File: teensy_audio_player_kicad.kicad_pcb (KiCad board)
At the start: 2 copper layers, 53.3 x 45.7 mm, 14 parts, among them J1 Conn_02x13_Odd_Even, J2 Conn_01x03_Female, J3 Conn_01x09_Male, Q1 2N3904, U1 Teensy3.6, U2 74LS373, U3 I2S_DAC

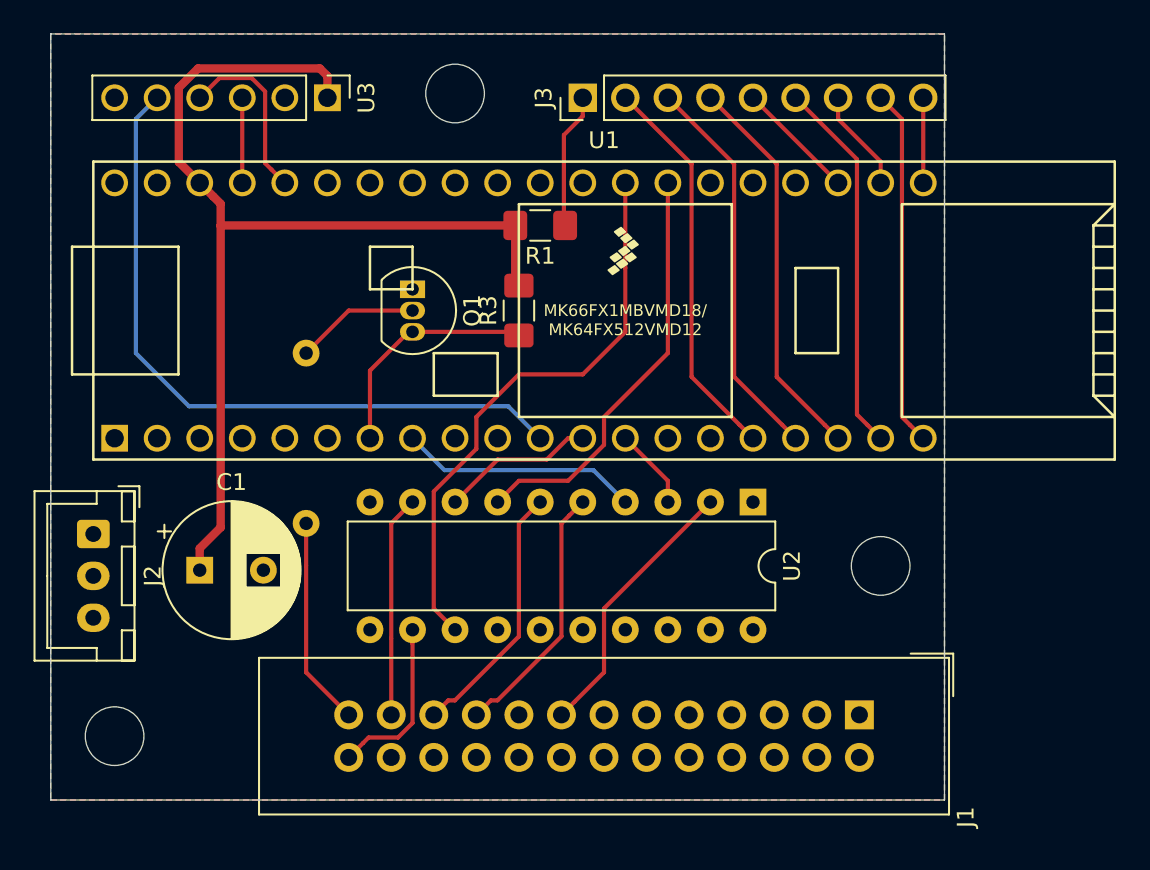
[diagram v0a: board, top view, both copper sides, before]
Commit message: update PCB for new version with teensy41
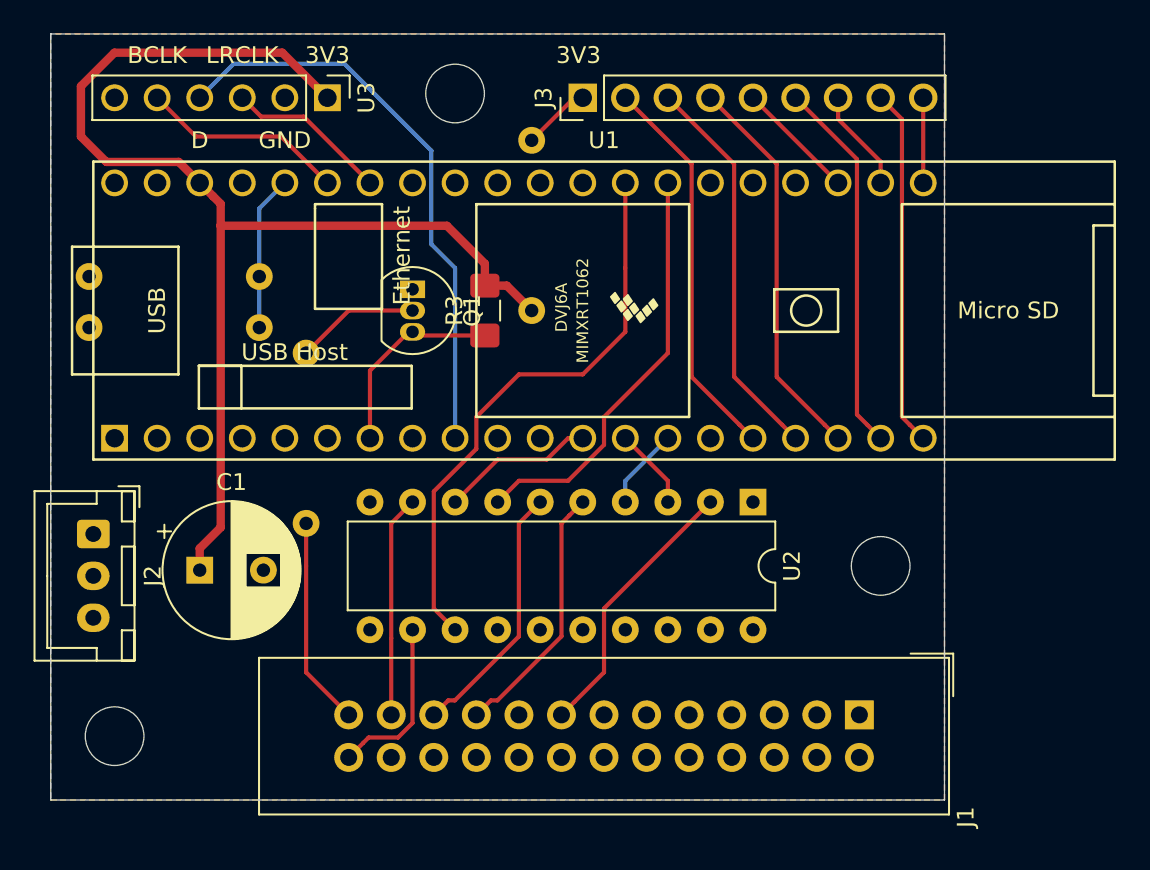
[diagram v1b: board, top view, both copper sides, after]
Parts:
- added R4: R-Device, Resistor_THT:R_Axial_DIN0207_L6.3mm_D2.5mm_P10.16mm_Horizontal, B.Cu at (88.6, 70.4)
- added R5: R-Device, Resistor_THT:R_Axial_DIN0207_L6.3mm_D2.5mm_P10.16mm_Horizontal, B.Cu at (88.6, 73.4)
- R1: footprint Resistor_SMD:R_1206_3216Metric_Pad1.42x1.75mm_HandSolder -> Resistor_THT:R_Axial_DIN0207_L6.3mm_D2.5mm_P10.16mm_Horizontal; moved to B.Cu
- U1: value Teensy3.6 -> Teensy4.1; footprint teensy_audio_player_kicad:Teensy35_36 -> teensy_audio_player_kicad:Teensy41
- moved R1 5.11 mm to (104.9, 72.4), turned to 90 degrees
- moved R3 2.03 mm to (102.1, 72.4)
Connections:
- net Net-(J3-Pad2) renamed /24
- net Net-(J3-Pad3) renamed /25
- net Net-(J3-Pad4) renamed /26
- net Net-(J3-Pad6) renamed /27
- net Net-(J3-Pad8) renamed /28
- net Net-(U1-Pad12) renamed /CS
- net Net-(U1-Pad13) renamed /MOSI
- J3 pad 5: Net-(J3-Pad5) -> /39
- J3 pad 7: Net-(J3-Pad7) -> /38
- J3 pad 9: Net-(J3-Pad9) -> /37
- R1 pad 1: Net-(J3-Pad1) -> +3V3
- R1 pad 2: +3V3 -> Net-(J3-Pad1)
- U1 pad 14: Net-(U1-Pad14) -> /CMD_DATA
- U1 pad 34: Net-(J3-Pad9) -> GND
- U1 pad 35: Net-(J3-Pad7) -> /SCK
- U1 pad 36: Net-(J3-Pad5) -> /RST
- U1 pad 39: GND -> Net-(U1-Pad39)
- U1 pad 46: Net-(U1-Pad46) -> +3V3
- U1 pad 47: Net-(U1-Pad47) -> GND
- U1 pad 48: Net-(U1-Pad48) -> VCC
- U2 pad 13: Net-(U1-Pad41) -> /RST
- U2 pad 4: Net-(U1-Pad8) -> /CMD_DATA
- U2 pad 7: Net-(U1-Pad40) -> /SCK
- U3 pad 3: Net-(U1-Pad50) -> Net-(U1-Pad42)
- U3 pad 4: Net-(U1-Pad49) -> Net-(U1-Pad9)
- U3 pad 5: Net-(U1-Pad11) -> Net-(U1-Pad43)
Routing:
- net Net-(U1-Pad11): track 42.0 -> 0.00 mm
- net Net-(U1-Pad9): track 0.00 -> 34.6 mm
- net Net-(U1-Pad41): track 34.2 -> 0.00 mm
- net /RST: track 0.00 -> 34.2 mm
- net Net-(U1-Pad40): track 25.0 -> 0.00 mm
- net /SCK: track 0.00 -> 25.0 mm
- net Net-(U1-Pad8): track 14.3 -> 0.00 mm
- net Net-(U1-Pad43): track 0.00 -> 12.9 mm
- net Net-(U1-Pad49): track 10.7 -> 0.00 mm
- net +3V3: track 62.9 -> 73.5 mm
- net Net-(U1-Pad42): track 0.00 -> 10.4 mm
- net Net-(R4-Pad1): track 0.00 -> 9.27 mm
- net Net-(J3-Pad5): track 7.18 -> 0.00 mm
- net /39: track 0.00 -> 7.18 mm
- net Net-(J3-Pad7): track 6.13 -> 0.00 mm
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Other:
- board text added: "3V3"
- board text added: "BCLK"
- board text added: "D"
- board text added: "GND"
- board text added: "LRCLK"
